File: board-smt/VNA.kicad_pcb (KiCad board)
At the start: 2 copper layers, 100 x 100 mm, 170 parts, among them J1 Conn_02x07_Odd_Even, J10 Conn_01x01, J11 Conn_01x01, J12 Conn_01x01, J13 Barrel_Jack, J14 Conn_01x01, J15 Conn_01x02, J16 Conn_01x01, J17 Conn_01x04, J18 Conn_01x01, J19 Conn_01x01, J2 Conn_Coaxial, J20 Conn_01x01, J21 Conn_01x01, J22 Conn_01x02, J24 USB_B, J3 Conn_01x01, J4 Conn_01x01, J5 Conn_01x01, J6 Conn_01x01, J7 Conn_01x01, J8 Conn_01x01, J9 Conn_Coaxial, Q3 S9018, SW1 SW_DPDT_x2, U1 SI5351A, U10 MT3608, U11 CN3052, U12 SI5351A, U2 LM339, U3 SA612, U4 SA612, U5 SA612, U6 LM358, U7 LM358, U8 AMS1117-3V3, U9 78M05_TO252, Y1 27 MHz, Y2 27 MHz

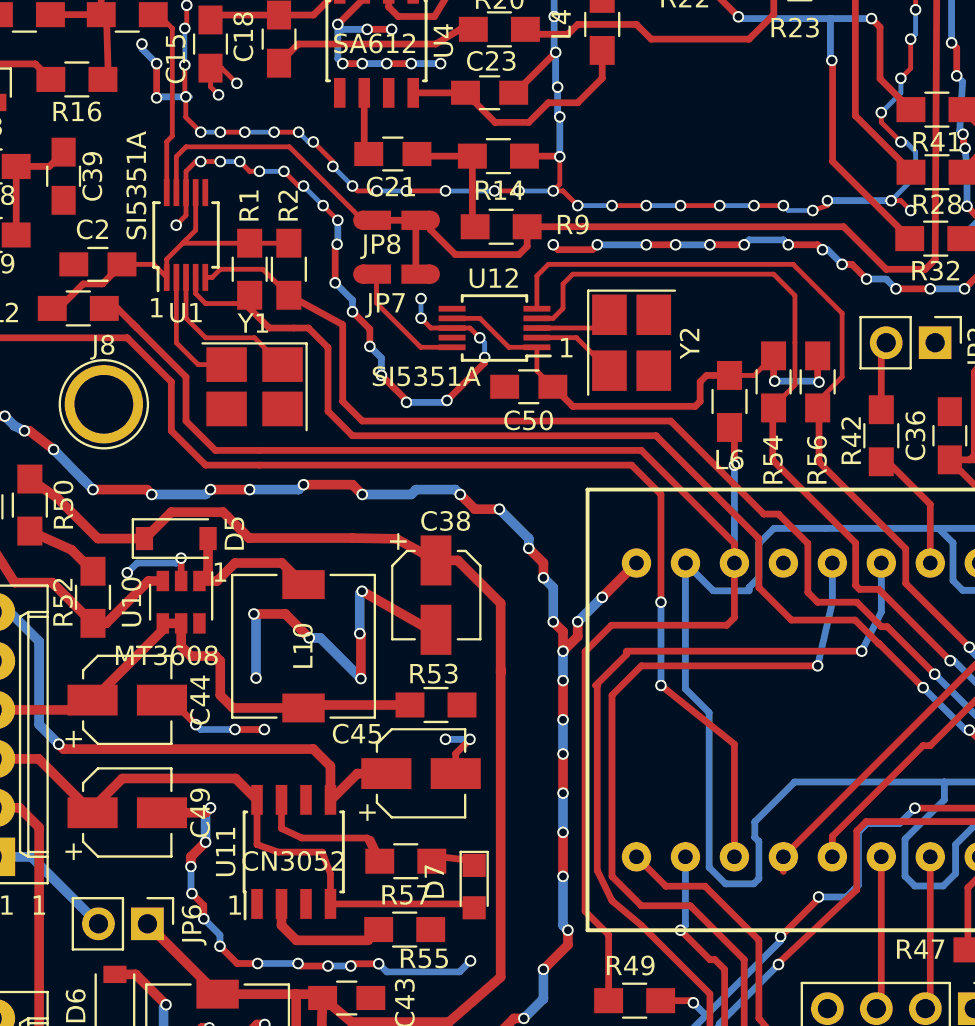
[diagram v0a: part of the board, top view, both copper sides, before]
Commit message: Slaved the second SI5351A to the first SI5351A
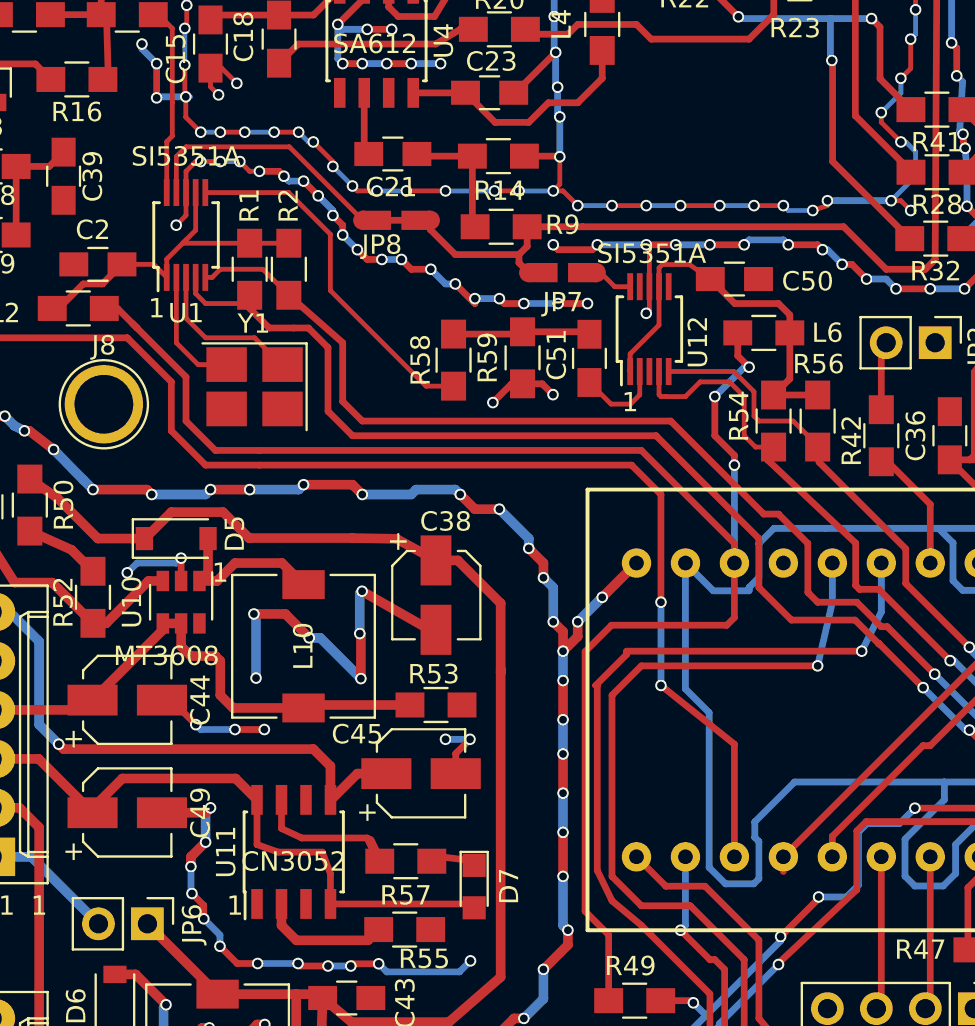
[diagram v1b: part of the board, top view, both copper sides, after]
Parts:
- removed Y2: 27 MHz, Crystals:Crystal_SMD_3225-4pin_3.2x2.5mm_HandSoldering
- added C51: 100 nF, Capacitors_SMD:C_0805_HandSoldering, F.Cu at (85.2, 99.6)
- added R58: 220R, Resistors_SMD:R_0805_HandSoldering, F.Cu at (78.1, 99.7)
- added R59: 100R, Resistors_SMD:R_0805_HandSoldering, F.Cu at (81.7, 99.6)
- moved C50 12.0 mm to (92.7, 95.5), turned to 180 degrees
- moved JP7 8.61 mm to (83.8, 95.2), turned to 180 degrees
- moved U12 8.04 mm to (88.3, 98.1), turned to 90 degrees
- moved L6 3.98 mm to (94.2, 98.3), turned to 180 degrees
- moved R54 2.03 mm to (94.7, 102.9)
- moved R56 2.03 mm to (97.0, 102.9)
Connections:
- U1 pad 6: (no net) -> Net-(R58-Pad1)
- U12 pad 3: Net-(U12-Pad3) -> (no net)
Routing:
- net Net-(R58-Pad1): track 0.00 -> 19.0 mm
- net SDA2: track 56.1 -> 40.3 mm
- net SCL2: track 59.3 -> 45.8 mm
- net Net-(C51-Pad2): track 0.00 -> 7.51 mm
- net +3V3: track 77.8 -> 84.1 mm, vias 1 -> 3
- net Net-(C50-Pad2): track 26.0 -> 20.8 mm, vias 2 -> 0
- net Net-(JP7-Pad1): track 6.37 -> 2.06 mm
- net Net-(U12-Pad3): track 4.05 -> 0.00 mm
- net Net-(JP7-Pad2): track 92.9 -> 91.3 mm
- net GND: track 1340.8 -> 1342.0 mm, vias 510 -> 513

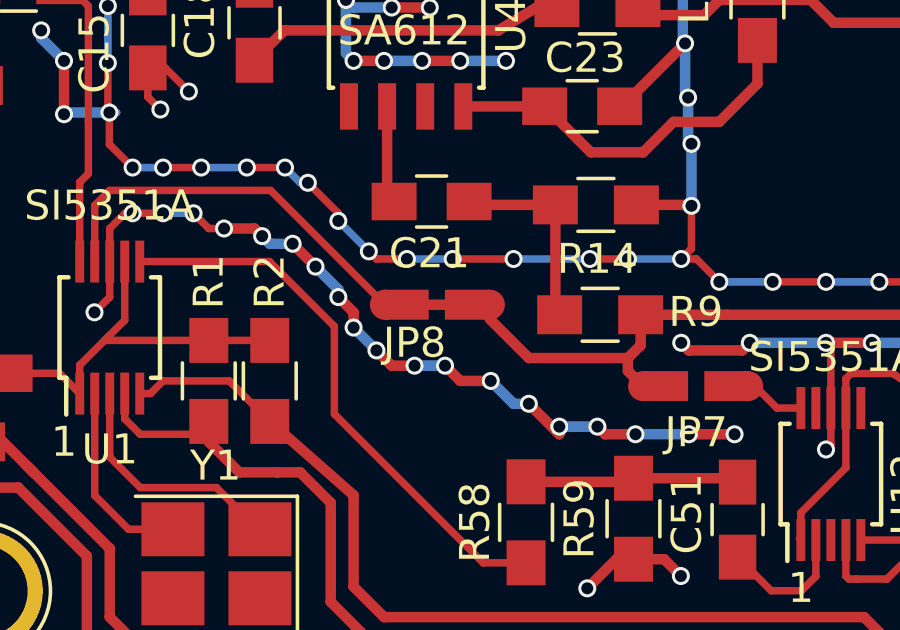
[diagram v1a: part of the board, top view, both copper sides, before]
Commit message: Moved jumper a little for lower parasitics
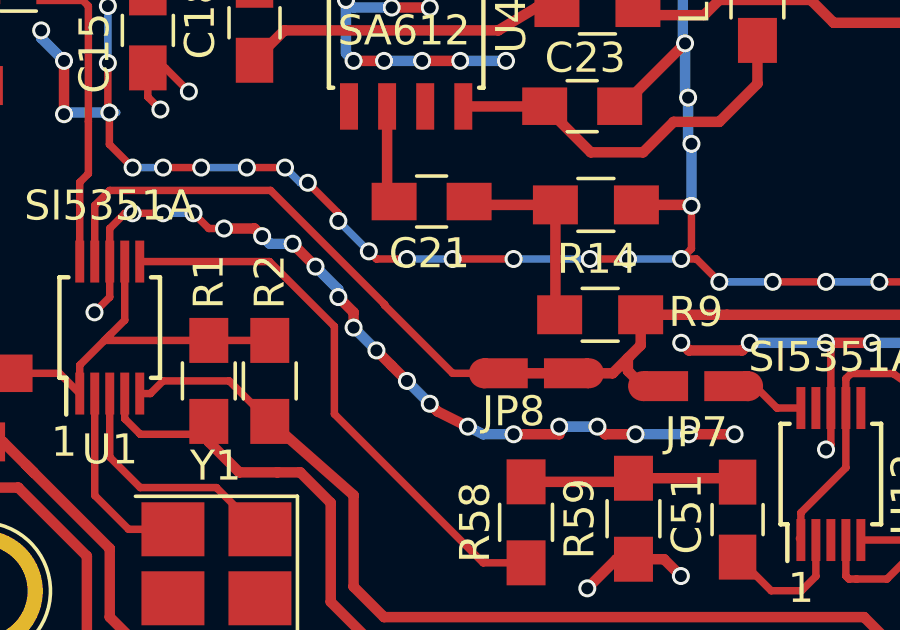
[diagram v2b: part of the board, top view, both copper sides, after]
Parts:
- moved JP8 4.02 mm to (78.5, 94.7)
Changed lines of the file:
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@@
     (thickness 1.6)
     (drawings 47)
-    (tracks 2896)
+    (tracks 2899)
     (zones 0)
     (modules 172)
@@
   )
   (setup
-    (last_trace_width 0.25)
+    (last_trace_width 0.35)
     (user_trace_width 0.35)
     (user_trace_width 0.5)
@@
       (effects (font (size 1 1) (thickness 0.15)))
     )
-    (fp_text value Jumper_NO_Small (at 0 -0.5 180) (layer F.Fab)
+    (fp_text value Jumper_NO_Small (at -0.792 -0.842 180) (layer F.Fab)
       (effects (font (size 1 1) (thickness 0.15)))
     )
@@
   )
   (module VNA:PAD_DEFAULT_OPEN (layer F.Cu)
-    (at 75.184 92.456)
+    (at 78.486 94.742)
     (fp_text reference JP8 (at -0.762 1.27) (layer F.SilkS)
       (effects (font (size 1 1) (thickness 0.15)))
@@
   (via (at 79.248 96.52) (size 0.6) (drill 0.4) (layers F.Cu B.Cu) (net 2))
   (segment (start 79.248 96.774) (end 79.248 96.52) (width 0.35) (layer F.Cu) (net 2))
-  (segment (start 78.232 95.758) (end 79.248 96.774) (width 0.35) (layer F.Cu) (net 2))
-  (via (at 78.232 95.758) (size 0.6) (drill 0.4) (layers F.Cu B.Cu) (net 2))
-  (segment (start 77.724 95.758) (end 78.232 95.758) (width 0.35) (layer B.Cu) (net 2))
-  (segment (start 76.962 94.996) (end 77.724 95.758) (width 0.35) (layer B.Cu) (net 2))
-  (via (at 76.962 94.996) (size 0.6) (drill 0.4) (layers F.Cu B.Cu) (net 2))
-  (segment (start 75.946 94.996) (end 76.962 94.996) (width 0.35) (layer F.Cu) (net 2))
-  (segment (start 75.438 94.488) (end 75.946 94.996) (width 0.35) (layer F.Cu) (net 2))
-  (via (at 75.438 94.488) (size 0.6) (drill 0.4) (layers F.Cu B.Cu) (net 2))
-  (segment (start 74.422 94.488) (end 75.438 94.488) (width 0.35) (layer B.Cu) (net 2))
-  (via (at 74.422 94.488) (size 0.6) (drill 0.4) (layers F.Cu B.Cu) (net 2))
-  (segment (start 73.66 94.488) (end 74.422 94.488) (width 0.35) (layer F.Cu) (net 2))
+  (segment (start 77.724 96.774) (end 79.248 96.774) (width 0.35) (layer F.Cu) (net 2))
+  (via (at 77.724 96.774) (size 0.6) (drill 0.4) (layers F.Cu B.Cu) (net 2))
+  (segment (start 76.708 96.774) (end 77.724 96.774) (width 0.35) (layer B.Cu) (net 2))
+  (segment (start 76.2 96.52) (end 76.708 96.774) (width 0.35) (layer B.Cu) (net 2))
+  (via (at 76.2 96.52) (size 0.6) (drill 0.4) (layers F.Cu B.Cu) (net 2))
+  (segment (start 75.184 96.012) (end 76.2 96.52) (width 0.35) (layer F.Cu) (net 2))
+  (segment (start 74.93 95.758) (end 75.184 96.012) (width 0.35) (layer F.Cu) (net 2))
+  (via (at 74.93 95.758) (size 0.6) (drill 0.4) (layers F.Cu B.Cu) (net 2))
+  (segment (start 74.168 94.996) (end 74.93 95.758) (width 0.35) (layer B.Cu) (net 2))
+  (via (at 74.168 94.996) (size 0.6) (drill 0.4) (layers F.Cu B.Cu) (net 2))
+  (segment (start 73.66 94.488) (end 74.168 94.996) (width 0.35) (layer F.Cu) (net 2))
   (segment (start 73.152 93.98) (end 73.66 94.488) (width 0.35) (layer F.Cu) (net 2))
   (via (at 73.152 93.98) (size 0.6) (drill 0.4) (layers F.Cu B.Cu) (net 2))
@@
   (segment (start 85.772 95.17) (end 86.502 95.9) (width 0.25) (layer F.Cu) (net 100))
   (segment (start 86.502 95.9) (end 87.3 95.9) (width 0.25) (layer F.Cu) (net 100))
+  (segment (start 79.486 94.742) (end 77.446 94.742) (width 0.35) (layer F.Cu) (net 101))
+  (segment (start 80.236 94.742) (end 81.026 94.742) (width 0.35) (layer F.Cu) (net 101))
+  (segment (start 81.026 94.742) (end 81.534 94.234) (width 0.35) (layer F.Cu) (net 101))
+  (segment (start 73.42 92.442) (end 73.42 92.47) (width 0.25) (layer F.Cu) (net 101))
+  (segment (start 75.692 94.742) (end 76.736 94.742) (width 0.25) (layer F.Cu) (net 101))
+  (segment (start 73.42 92.47) (end 75.692 94.742) (width 0.25) (layer F.Cu) (net 101))
   (segment (start 81.534 94.234) (end 81.534 94.664) (width 0.35) (layer F.Cu) (net 101))
   (segment (start 81.534 94.664) (end 82.04 95.17) (width 0.35) (layer F.Cu) (net 101))
-  (segment (start 76.934 92.456) (end 76.934 92.936) (width 0.35) (layer F.Cu) (net 101))
-  (segment (start 76.934 92.936) (end 78.232 94.234) (width 0.35) (layer F.Cu) (net 101))
-  (segment (start 78.232 94.234) (end 81.534 94.234) (width 0.35) (layer F.Cu) (net 101))
   (segment (start 81.534 94.234) (end 81.95944 93.80856) (width 0.35) (layer F.Cu) (net 101))
   (segment (start 81.95944 93.80856) (end 81.95944 92.79128) (width 0.35) (layer F.Cu) (net 101))
-  (segment (start 74.144 92.456) (end 76.184 92.456) (width 0.35) (layer F.Cu) (net 101))
   (segment (start 63.762 91.018) (end 63.762 89.146) (width 0.25) (layer F.Cu) (net 101))
-  (segment (start 69.624 88.646) (end 73.434 92.456) (width 0.25) (layer F.Cu) (net 101))
+  (segment (start 69.624 88.646) (end 73.42 92.442) (width 0.25) (layer F.Cu) (net 101))
+  (segment (start 73.42 92.442) (end 73.434 92.456) (width 0.25) (layer F.Cu) (net 101))
   (segment (start 64.262 88.646) (end 69.624 88.646) (width 0.25) (layer F.Cu) (net 101))
   (segment (start 63.762 89.146) (end 64.262 88.646) (width 0.25) (layer F.Cu) (net 101))

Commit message: JLCPCB order 2019-11-22
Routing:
- net GND: track 1341.8 -> 1353.1 mm, vias 513 -> 520
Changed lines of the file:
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@@
     (thickness 1.6)
     (drawings 47)
-    (tracks 2899)
+    (tracks 2920)
     (zones 0)
     (modules 172)
@@
   )
   (setup
-    (last_trace_width 0.35)
+    (last_trace_width 0.25)
     (user_trace_width 0.35)
     (user_trace_width 0.5)
@@
   (segment (start 103.23164 58.0844) (end 102.27564 57.1284) (width 0.35) (layer F.Cu) (net 1) (status 20))
   (segment (start 106.0704 78.59904) (end 106.0704 78.68412) (width 0.35) (layer F.Cu) (net 1))
+  (segment (start 57.912 91.42) (end 58.4 91.42) (width 0.35) (layer F.Cu) (net 2))
+  (segment (start 58.4 91.42) (end 58.928 91.948) (width 0.35) (layer F.Cu) (net 2))
+  (segment (start 58.928 91.948) (end 59.69 91.948) (width 0.35) (layer F.Cu) (net 2))
+  (via (at 59.69 91.948) (size 0.6) (drill 0.4) (layers F.Cu B.Cu) (net 2))
+  (segment (start 59.69 91.948) (end 60.96 91.948) (width 0.35) (layer B.Cu) (net 2))
+  (via (at 60.96 91.948) (size 0.6) (drill 0.4) (layers F.Cu B.Cu) (net 2))
+  (segment (start 60.96 91.948) (end 61.214 91.694) (width 0.35) (layer F.Cu) (net 2))
+  (segment (start 61.214 91.694) (end 61.214 90.932) (width 0.35) (layer F.Cu) (net 2))
+  (via (at 61.214 90.932) (size 0.6) (drill 0.4) (layers F.Cu B.Cu) (net 2))
+  (segment (start 54.544 86.344) (end 55.102 86.344) (width 0.35) (layer F.Cu) (net 2))
+  (via (at 60.452 88.138) (size 0.6) (drill 0.4) (layers F.Cu B.Cu) (net 2))
+  (segment (start 59.69 88.138) (end 60.452 88.138) (width 0.35) (layer B.Cu) (net 2))
+  (segment (start 59.182 87.63) (end 59.69 88.138) (width 0.35) (layer B.Cu) (net 2))
+  (via (at 59.182 87.63) (size 0.6) (drill 0.4) (layers F.Cu B.Cu) (net 2))
+  (segment (start 57.404 87.63) (end 59.182 87.63) (width 0.35) (layer F.Cu) (net 2))
+  (segment (start 56.896 87.122) (end 57.404 87.63) (width 0.35) (layer F.Cu) (net 2))
+  (via (at 56.896 87.122) (size 0.6) (drill 0.4) (layers F.Cu B.Cu) (net 2))
+  (segment (start 55.88 87.122) (end 56.896 87.122) (width 0.35) (layer B.Cu) (net 2))
+  (segment (start 55.626 86.868) (end 55.88 87.122) (width 0.35) (layer B.Cu) (net 2))
+  (via (at 55.626 86.868) (size 0.6) (drill 0.4) (layers F.Cu B.Cu) (net 2))
+  (segment (start 55.102 86.344) (end 55.626 86.868) (width 0.35) (layer F.Cu) (net 2))
   (segment (start 88.3 95.9) (end 88.3 97.12) (width 0.25) (layer F.Cu) (net 2))
   (via (at 88.138 97.282) (size 0.6) (drill 0.4) (layers F.Cu B.Cu) (net 2))
@@
   (via (at 65.278 65.278) (size 0.6) (drill 0.4) (layers F.Cu B.Cu) (net 2))
   (segment (start 65.278 64.77) (end 65.278 65.278) (width 0.35) (layer B.Cu) (net 2))
-  (segment (start 65.786 64.262) (end 65.278 64.77) (width 0.35) (layer B.Cu) (net 2))
-  (via (at 65.786 64.262) (size 0.6) (drill 0.4) (layers F.Cu B.Cu) (net 2))
-  (segment (start 66.802 63.246) (end 65.786 64.262) (width 0.35) (layer F.Cu) (net 2))
-  (via (at 66.802 63.246) (size 0.6) (drill 0.4) (layers F.Cu B.Cu) (net 2))
-  (segment (start 67.564 63.246) (end 66.802 63.246) (width 0.35) (layer B.Cu) (net 2))
+  (segment (start 65.786 63.754) (end 65.278 64.77) (width 0.35) (layer B.Cu) (net 2))
+  (via (at 65.786 63.754) (size 0.6) (drill 0.4) (layers F.Cu B.Cu) (net 2))
+  (segment (start 66.802 62.992) (end 65.786 63.754) (width 0.35) (layer F.Cu) (net 2))
+  (via (at 66.802 62.992) (size 0.6) (drill 0.4) (layers F.Cu B.Cu) (net 2))
+  (segment (start 67.564 63.246) (end 66.802 62.992) (width 0.35) (layer B.Cu) (net 2))
   (segment (start 68.072 62.738) (end 67.564 63.246) (width 0.35) (layer B.Cu) (net 2))
   (via (at 68.072 62.738) (size 0.6) (drill 0.4) (layers F.Cu B.Cu) (net 2))
@@
   (segment (start 68.706 58.928) (end 67.818 58.928) (width 0.35) (layer F.Cu) (net 38) (status 10))
   (segment (start 64.008 60.96) (end 60.198 64.262) (width 0.35) (layer F.Cu) (net 38) (status 20))
-  (segment (start 65.786 60.96) (end 64.008 60.96) (width 0.35) (layer F.Cu) (net 38))
-  (segment (start 67.818 58.928) (end 65.786 60.96) (width 0.35) (layer F.Cu) (net 38))
+  (segment (start 67.31 59.69) (end 64.008 60.96) (width 0.35) (layer F.Cu) (net 38))
+  (segment (start 67.818 58.928) (end 67.31 59.69) (width 0.35) (layer F.Cu) (net 38))
   (segment (start 60.198 64.262) (end 60.198 65.532) (width 0.35) (layer F.Cu) (net 38) (status 30))
   (segment (start 60.198 65.532) (end 60.198 64.516) (width 0.35) (layer F.Cu) (net 38) (status 30))
